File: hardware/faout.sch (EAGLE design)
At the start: 106 parts, among them IC2 MT48LC64M4A2, Q1 12MHz, Q2 ASFL, U1 LTC3419EMS, U10 REF102AU, U2 93C46B, U3 FLASH-SPI-25XXSMD1, U4 6SLX9TQG144, U5 OPA2277UA/2K5E4, U6 DAC8811DGK, U7 REF102AU, U8 OPA2277UA/2K5E4, U9 DAC8811DGK

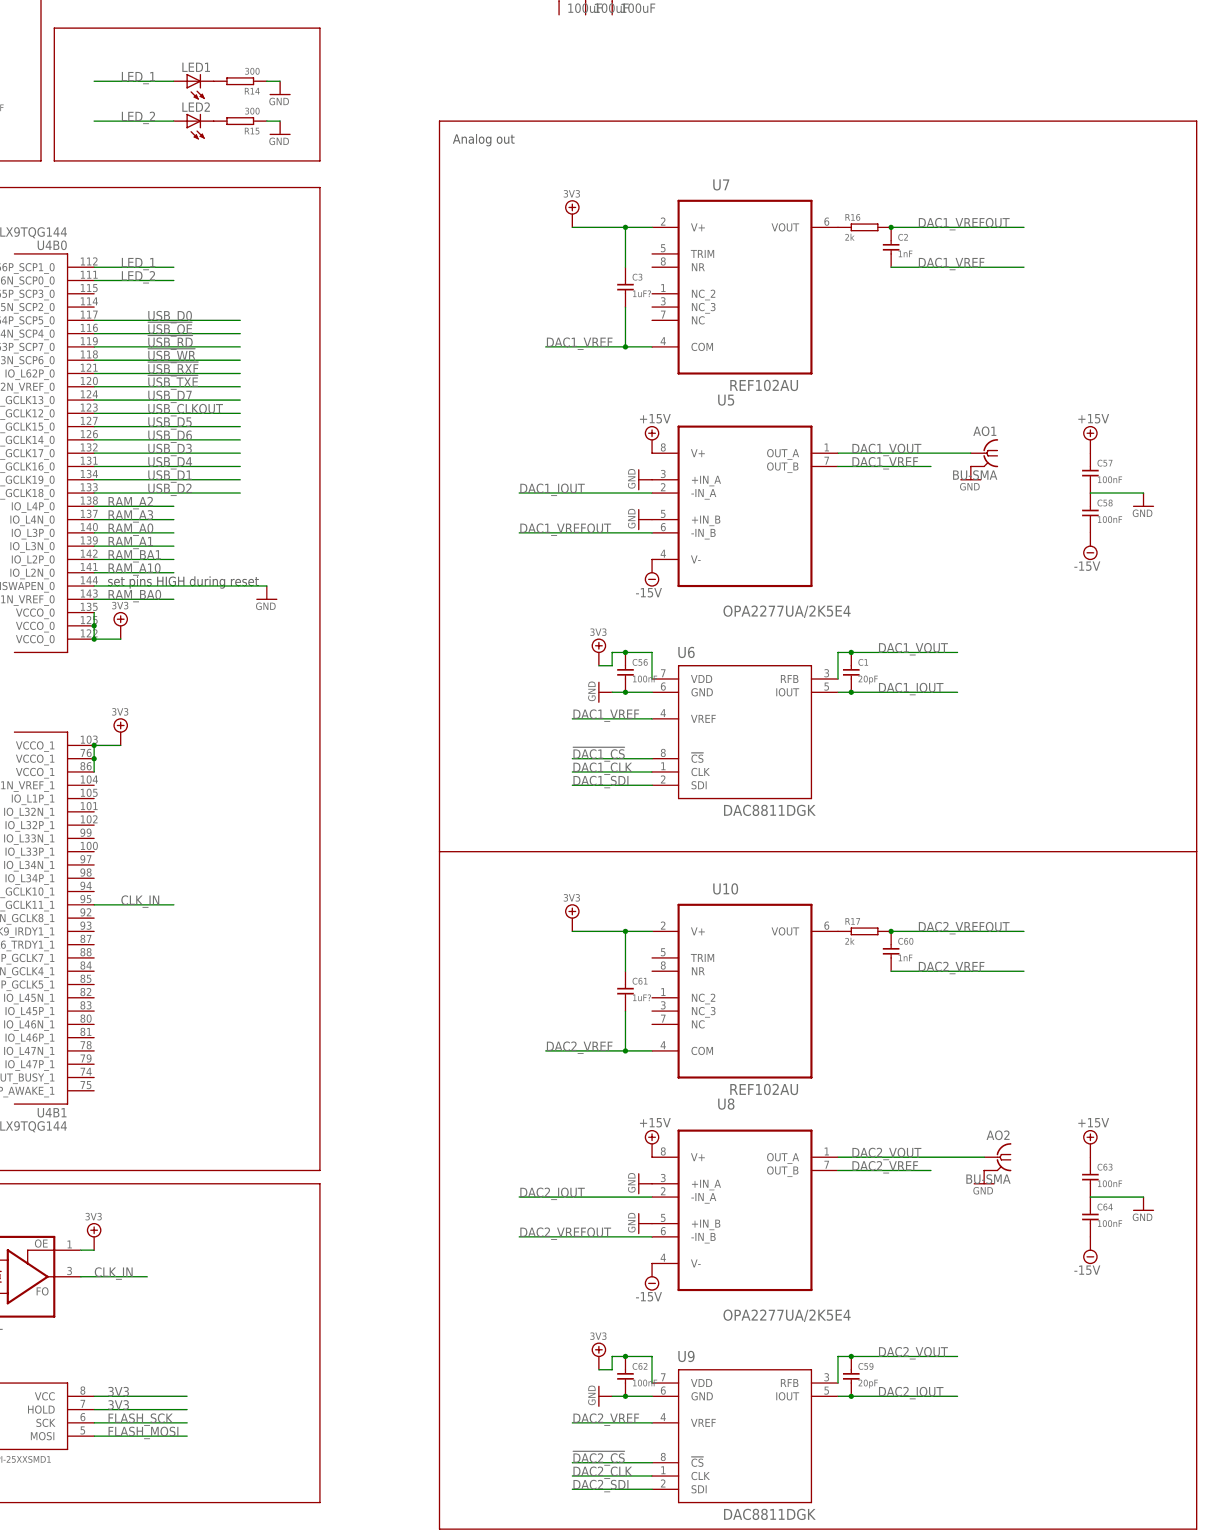
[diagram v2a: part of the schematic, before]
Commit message: Connected DACs to power and FPGA.
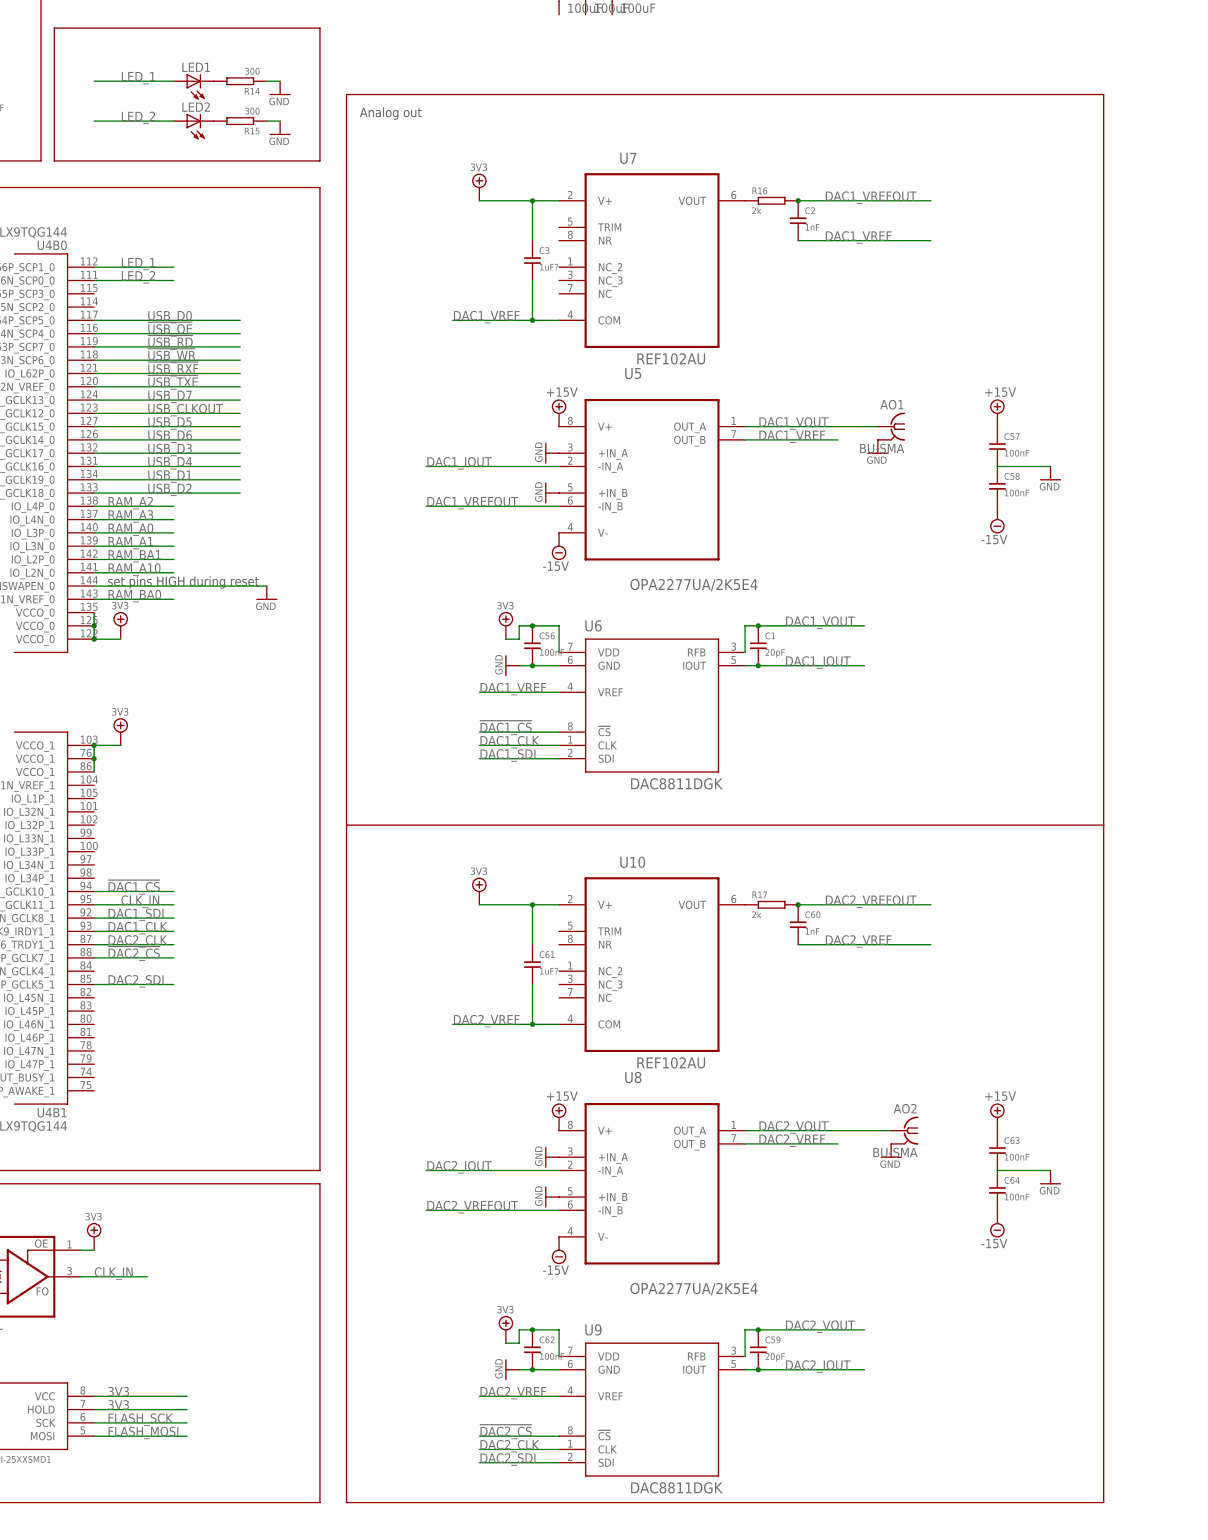
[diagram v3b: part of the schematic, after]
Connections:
- net !DAC1_CS: now also U4B1.IO_L40N_GCLK10_1
- net !DAC2_CS: now also U4B1.IO_L42P_GCLK7_1
- net DAC1_CLK: now also U4B1.IO_L41P_GCLK9_IRDY1_1
- net DAC1_SDI: now also U4B1.IO_L41N_GCLK8_1
- net DAC2_CLK: now also U4B1.IO_L42N_GCLK6_TRDY1_1
- net DAC2_SDI: now also U4B1.IO_L43P_GCLK5_1
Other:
- moved on the sheet: AO1, AO2, C1, C2, C3, C56, C57, C58, C59, C60, C61, C62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

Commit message: Add parts for ADC conversion.
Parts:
- added AI1: BU-SMA, analog_out_lib:BU-SMA
- added C65: 22uF, resistor:C-EUC1206
- added C66, C67: 100nF, faout:C_EU0603
- added U11: DAC8811DGK, faout:DAC8811DGK
- added U12: MCP1700T-2502E/TT, faout:MCP1700T-2502E/TT
- added U13: AD7980ARMZ, faout:AD7980ARMZ
- added U14: ADR435ARZ, faout:ADR435ARZ
- C1: value 20pF -> 3.3uF
- C12: value 100nF -> 10uF/10V; device faout:C_EU0603 -> faout:C_EU0805
- C17, C18: value 100nF -> 470nF
- C19, C20: value 100uF -> 4.7uF; device rcl:C-EUC1210K -> faout:C_EU0603
- C2: value 1nF -> 18pF
- C21: value 100uF -> 10nF; device rcl:C-EUC1210K -> faout:C_EU0603
- C22, C23: value 470nF -> 22uF/6V3; device faout:C_EU0603 -> faout:C_EU0805
- C24, C44: value 4.7uF -> 10nF
- C27, C33, C35, C37, C39, C45: value 4.7uF -> 470nF
- C28, C29, C31, C34, C38, C46: value 470nF -> 4.7uF
- C3: value 1uF? -> 18pF
- C4: value 3.3uF -> 4.7uF
- C5: value 18pF -> 100nF
- C50, C52: value 10nF -> 1uF?
- C51: value 10nF -> 100nF
- C53: value 10uF/10V -> 100nF; device faout:C_EU0805 -> faout:C_EU0603
- C54, C55: value 22uF/6V3 -> 1uF; device faout:C_EU0805 -> faout:C_EU0603
- C57, C58: value 100nF -> 20pF
- C59: value 20pF -> 1nF
- C6: value 18pF -> 4.7uF
- C61: value 1uF? -> 100nF
- C7, C9: value 4.7uF -> 100nF
- IC1: value (none) -> MT48LC64M4A2; device ftdichip-3:FT2232HL -> faout:MT48LC64M4A2
- IC2: value MT48LC64M4A2 -> (none); device faout:MT48LC64M4A2 -> ftdichip-3:FT2232HL
- L1, L2: value 3.3uH -> (none); device Bogdan_Commons:L_VLS3015 -> faout:R_EU0603
- L3, L4: value (none) -> 3.3uH; device faout:R_EU0603 -> Bogdan_Commons:L_VLS3015
- R1, R2, R4: value 1K5 1% -> 10k
- R10: value 12k -> 1K5 1%
- R11: value 0 -> 6K8 1%
- R12: value 0 -> 1K5 1%
- R3: value 6K8 1% -> 2.2k
- R5: value 10k -> 1k
- R6: value 10k -> 12k
- R7: value 2.2k -> 0
- R8: value 10k -> 0
- R9: value 1k -> 1K5 1%
- U1: value LTC3419EMS -> 93C46B; device Bogdan_Commons:LTC3419EMS -> Bogdan_Commons:DIGITAL-EEPROM-MICROWIRE-6P_SOT23
- U10, U7: value REF102AU -> OPA2277UA/2K5E4; device faout:REF102AU -> faout:OPA2277UA/2K5E4
- U2: value 93C46B -> LTC3419EMS; device Bogdan_Commons:DIGITAL-EEPROM-MICROWIRE-6P_SOT23 -> Bogdan_Commons:LTC3419EMS
- U5: value OPA2277UA/2K5E4 -> AD8220ARMZ; device faout:OPA2277UA/2K5E4 -> faout:AD8220ARMZ
- U6, U9: value DAC8811DGK -> REF102AU; device faout:DAC8811DGK -> faout:REF102AU
- U8: value OPA2277UA/2K5E4 -> DAC8811DGK; device faout:OPA2277UA/2K5E4 -> faout:DAC8811DGK
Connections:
- new net 2V5: C55.P$1, U12.VOUT, U13.VDD
- new net ADC1_CNV: U13.CNV
- new net ADC1_REF: C65.1, U13.REF, U14.VOUT
- new net ADC1_SCK: U13.SCK
- new net ADC1_SDI: U13.SDI
- new net ADC1_SDO: U13.SDO
- new net N$11: AI1.2, U5.-IN
- new net N$12: C54.P$1, U12.VIN
- new net N$9: AI1.1, U5.+IN
- net !DAC1_CS: now also U8.!CS; no longer U6.!CS
- net !DAC2_CS: now also U11.!CS; no longer U9.!CS
- net !RAM_CAS: now also IC1G$1.!CAS; no longer IC2G$1.!CAS
- net !RAM_RAS: now also IC1G$1.!RAS; no longer IC2G$1.!RAS
- net !RAM_WE: now also IC1G$1.!WE; no longer IC2G$1.!WE
- net !USB_OE: now also IC2.ACBUS6; no longer IC1.ACBUS6
- net !USB_RD: now also IC2.ACBUS2; no longer IC1.ACBUS2
- net !USB_RESET: now also IC2.-RESET, R5.P$1; no longer IC1.-RESET, R9.P$1
- net !USB_RXF: now also IC2.ACBUS0; no longer IC1.ACBUS0
- net !USB_TXE: now also IC2.ACBUS1; no longer IC1.ACBUS1
- net !USB_WR: now also IC2.ACBUS3; no longer IC1.ACBUS3
- net +15V: now also C56.P$1, C61.P$1, C66.P$1, U10.V+, U14.VIN, U5.+VS, U7.V+; no longer C57.P$1, U5.V+, U8.V+
- net -15V: now also C62.P$2, C67.P$2, U10.V-, U5.-VS, U7.V-; no longer C58.P$2, U5.V-, U8.V-
- net 1V2: now also C23.P$1, C26.P$1, C28.P$1, C30.P$1, C31.P$1, L4.2, R12.P$2; no longer C34.P$1, C35.P$1, C36.P$1, C37.P$1, C55.P$1, L2.2, R4.P$2
- net 1V8: now also C1.P$1, C10.P$1, C11.P$1, C9.P$1, IC2.VCORE@1, IC2.VCORE@2, IC2.VCORE@3, IC2.VREGOUT; no longer C12.P$1, C13.P$1, C14.P$1, C4.P$1, IC1.VCORE@1, IC1.VCORE@2, IC1.VCORE@3, IC1.VREGOUT
- net 3V3: now also C13.P$1, C14.P$1, C19.P$1, C20.P$1, C21.P$1, C34.P$1, C35.P$1, C36.P$1, C37.P$1, C5.P$1, C53.P$1, IC1P.VDD@1, IC1P.VDD@2, IC1P.VDD@3, IC1P.VDDQ@1, IC1P.VDDQ@2, IC1P.VDDQ@3, IC1P.VDDQ@4, IC2.ACBUS4, IC2.VCCIO@1, IC2.VCCIO@2, IC2.VCCIO@3, IC2.VCCIO@4, IC2.VREGIN, L1.P$1, L2.P$1, L3.2, R1.P$2, R11.P$2, R2.P$2, R4.P$2, U1.VCC, U11.VDD, U2.RUN2, U6.V+, U8.VDD, U9.V+; no longer C23.P$1, C26.P$1, C28.P$1, C3.P$1, C30.P$1, C31.P$1, C54.P$1, C56.P$1, C61.P$1, C62.P$1, C8.P$1, IC1.ACBUS4, IC1.VCCIO@1, IC1.VCCIO@2, IC1.VCCIO@3, IC1.VCCIO@4, IC1.VREGIN, IC2P.VDD@1, IC2P.VDD@2, IC2P.VDD@3, IC2P.VDDQ@1, IC2P.VDDQ@2, IC2P.VDDQ@3, IC2P.VDDQ@4, L1.2, L3.P$1, L4.P$1, R3.P$2, R6.P$2, R8.P$2, R9.P$2, U1.RUN2, U10.V+, U2.VCC, U6.VDD, U7.V+, U9.VDD
- net 5V0: now also C12.P$1, R7.P$1, U2.MODE, U2.RUN1, U2.VIN; no longer C53.P$1, R12.P$1, U1.MODE, U1.RUN1, U1.VIN
- net DAC1_CLK: now also U8.CLK; no longer U6.CLK
- net DAC1_IOUT: now also C57.P$2, U7.-IN_A, U8.IOUT; no longer C1.P$2, U5.-IN_A, U6.IOUT
- net DAC1_SDI: now also U8.SDI; no longer U6.SDI
- net DAC1_VOUT: now also C57.P$1, U7.OUT_A, U8.RFB; no longer C1.P$1, U5.OUT_A, U6.RFB
- net DAC1_VREF: now also C50.P$2, C59.P$2, U6.COM, U7.OUT_B, U8.VREF; no longer C2.P$2, C3.P$2, U5.OUT_B, U6.VREF, U7.COM
- net DAC1_VREFOUT: now also C59.P$1, U7.-IN_B; no longer C2.P$1, U5.-IN_B
- net DAC2_CLK: now also U11.CLK; no longer U9.CLK
- net DAC2_IOUT: now also C58.P$2, U10.-IN_A, U11.IOUT; no longer C59.P$2, U8.-IN_A, U9.IOUT
- net DAC2_SDI: now also U11.SDI; no longer U9.SDI
- net DAC2_VOUT: now also C58.P$1, U10.OUT_A, U11.RFB; no longer C59.P$1, U8.OUT_A, U9.RFB
- net DAC2_VREF: now also C52.P$2, U10.OUT_B, U11.VREF, U9.COM; no longer C61.P$2, U10.COM, U8.OUT_B, U9.VREF
- net DAC2_VREFOUT: now also U10.-IN_B; no longer U8.-IN_B
- net EECS: now also IC2.EECS, R1.P$1, U1.CS; no longer IC1.EECS, R5.P$1, U2.CS
- net EEDATA: now also IC2.EEDATA, R3.P$1, R4.P$1, U1.DI; no longer IC1.EEDATA, R7.P$1, R8.P$1, U2.DI
- net EESK: now also IC2.EESK, R2.P$1, U1.CLK; no longer IC1.EESK, R6.P$1, U2.CLK
- net FB_1V2: now also R10.P$2, R12.P$1, U2.VFB2; no longer R2.P$2, R4.P$1, U1.VFB2
- net FB_3V3: now also R11.P$1, R9.P$2, U2.VFB1; no longer R1.P$2, R3.P$1, U1.VFB1
- net GND: now also C1.P$2, C19.P$2, C2.P$2, C20.P$2, C21.P$2, C3.P$2, C61.P$2, C62.P$1, C65.2, C66.P$2, C67.P$1, IC1P.VSS@1, IC1P.VSS@2, IC1P.VSS@3, IC1P.VSSQ@1, IC1P.VSSQ@2, IC1P.VSSQ@3, IC1P.VSSQ@4, IC2.AGND, IC2.GND@1, IC2.GND@2, IC2.GND@3, IC2.GND@4, IC2.GND@5, IC2.GND@6, IC2.GND@7, IC2.GND@8, IC2.TEST, R10.P$1, R6.P$2, R8.P$1, R9.P$1, U1.GND, U10.+IN_A, U10.+IN_B, U11.GND, U12.GND, U13.GND, U13.IN-, U14.GND, U2.GND@5, U2.GND@6, U5.REF, U7.+IN_A, U7.+IN_B, U8.GND; no longer C50.P$2, C52.P$2, C57.P$2, C58.P$1, C62.P$2, IC1.AGND, IC1.GND@1, IC1.GND@2, IC1.GND@3, IC1.GND@4, IC1.GND@5, IC1.GND@6, IC1.GND@7, IC1.GND@8, IC1.TEST, IC2P.VSS@1, IC2P.VSS@2, IC2P.VSS@3, IC2P.VSSQ@1, IC2P.VSSQ@2, IC2P.VSSQ@3, IC2P.VSSQ@4, R1.P$1, R10.P$2, R11.P$1, R2.P$1, U1.GND@5, U1.GND@6, U2.GND, U5.+IN_A, U5.+IN_B, U6.GND, U8.+IN_A, U8.+IN_B, U9.GND
- net N$1: now also C2.P$1, IC2.XTIN; no longer C5.P$1, IC1.XTIN
- net N$10: now also U6.VOUT; no longer U7.VOUT
- net N$2: now also C3.P$1, IC2.XTOUT; no longer C6.P$1, IC1.XTOUT
- net N$5: now also C4.P$1, IC2.VPHY, L2.P$2; no longer C10.P$1, IC1.VPHY, L4.P$2
- net N$6: now also R3.P$2, U1.DO; no longer R7.P$2, U2.DO
- net N$7: now also C6.P$1, C8.P$1, IC2.VPLL, L1.P$2; no longer C11.P$1, C9.P$1, IC1.VPLL, L3.P$2
- net N$8: now also U9.VOUT; no longer U10.VOUT
- net RAM_A0: now also IC1G$1.A0; no longer IC2G$1.A0
- net RAM_A1: now also IC1G$1.A1; no longer IC2G$1.A1
- net RAM_A10: now also IC1G$1.A10; no longer IC2G$1.A10
- net RAM_A11: now also IC1G$1.A11; no longer IC2G$1.A11
- net RAM_A12: now also IC1G$1.A12; no longer IC2G$1.A12
- net RAM_A2: now also IC1G$1.A2; no longer IC2G$1.A2
- net RAM_A3: now also IC1G$1.A3; no longer IC2G$1.A3
- net RAM_A4: now also IC1G$1.A4; no longer IC2G$1.A4
- net RAM_A5: now also IC1G$1.A5; no longer IC2G$1.A5
- net RAM_A6: now also IC1G$1.A6; no longer IC2G$1.A6
- net RAM_A7: now also IC1G$1.A7; no longer IC2G$1.A7
- net RAM_A8: now also IC1G$1.A8; no longer IC2G$1.A8
- net RAM_A9: now also IC1G$1.A9; no longer IC2G$1.A9
- net RAM_BA0: now also IC1G$1.BA0; no longer IC2G$1.BA0
- net RAM_BA1: now also IC1G$1.BA1; no longer IC2G$1.BA1
- net RAM_CKE: now also IC1G$1.CKE; no longer IC2G$1.CKE
- net RAM_CLK: now also IC1G$1.CLK; no longer IC2G$1.CLK
- net RAM_CS: now also IC1G$1.\CS; no longer IC2G$1.\CS
- net RAM_DQ0: now also IC1G$1.DQ0; no longer IC2G$1.DQ0
- net RAM_DQ1: now also IC1G$1.DQ1; no longer IC2G$1.DQ1
- net RAM_DQ10: now also IC1G$1.DQ10; no longer IC2G$1.DQ10
- net RAM_DQ11: now also IC1G$1.DQ11; no longer IC2G$1.DQ11
- net RAM_DQ12: now also IC1G$1.DQ12; no longer IC2G$1.DQ12
- net RAM_DQ13: now also IC1G$1.DQ13; no longer IC2G$1.DQ13
- net RAM_DQ14: now also IC1G$1.DQ14; no longer IC2G$1.DQ14
- net RAM_DQ15: now also IC1G$1.DQ15; no longer IC2G$1.DQ15
- net RAM_DQ2: now also IC1G$1.DQ2; no longer IC2G$1.DQ2
- net RAM_DQ3: now also IC1G$1.DQ3; no longer IC2G$1.DQ3
- net RAM_DQ4: now also IC1G$1.DQ4; no longer IC2G$1.DQ4
- net RAM_DQ5: now also IC1G$1.DQ5; no longer IC2G$1.DQ5
- net RAM_DQ6: now also IC1G$1.DQ6; no longer IC2G$1.DQ6
- net RAM_DQ7: now also IC1G$1.DQ7; no longer IC2G$1.DQ7
- net RAM_DQ8: now also IC1G$1.DQ8; no longer IC2G$1.DQ8
- net RAM_DQ9: now also IC1G$1.DQ9; no longer IC2G$1.DQ9
- net RAM_DQMH: now also IC1G$1.DQMH; no longer IC2G$1.DQMH
- net RAM_DQML: now also IC1G$1.DQML; no longer IC2G$1.DQML
- net SW_1V2: now also L4.1, U2.SW2; no longer L2.1, U1.SW2
- net SW_3V3: now also L3.1, U2.SW1; no longer L1.1, U1.SW1
- net TCK: now also IC2.BDBUS0; no longer IC1.BDBUS0
- net TDI: now also IC2.BDBUS1; no longer IC1.BDBUS1
- net TDO: now also IC2.BDBUS2; no longer IC1.BDBUS2
- net TMS: now also IC2.BDBUS3; no longer IC1.BDBUS3
- net USB_CLKOUT: now also IC2.ACBUS5; no longer IC1.ACBUS5
- net USB_D0: now also IC2.ADBUS0; no longer IC1.ADBUS0
- net USB_D1: now also IC2.ADBUS1; no longer IC1.ADBUS1
- net USB_D2: now also IC2.ADBUS2; no longer IC1.ADBUS2
- net USB_D3: now also IC2.ADBUS3; no longer IC1.ADBUS3
- net USB_D4: now also IC2.ADBUS4; no longer IC1.ADBUS4
- net USB_D5: now also IC2.ADBUS5; no longer IC1.ADBUS5
- net USB_D6: now also IC2.ADBUS6; no longer IC1.ADBUS6
- net USB_D7: now also IC2.ADBUS7; no longer IC1.ADBUS7
- net USB_DM: now also IC2.D-; no longer IC1.D-
- net USB_DP: now also IC2.D+; no longer IC1.D+
- net USB_GND: now also R8.P$2; no longer R11.P$2
- net USB_REF: now also IC2.REF, R6.P$1; no longer IC1.REF, R10.P$1
- net USB_V: now also R7.P$2; no longer R12.P$2
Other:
- moved on the sheet: C1, C10, C11, C12, C13, C14, C15, C16, C17, C18, C19, C2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

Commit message: Finalize USB and ADC layout.
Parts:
- added C68, C69: 100nF, faout:C_EU0603
- added C70: 114pF, faout:C_EU0603
- added C71: 11.4pF, faout:C_EU0603
- added JP3: (no value), pinhead:PINHD-1X2
- added L5: (no value), faout:R_EU0603
- added R18, R19: 7.47k, faout:R_EU0603
- added R20: 134k, faout:R_EU0603
- added U15: AD8627AKSZ-R2, faout:AD8627AKSZ-R2
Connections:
- removed net +15V: C56.P$1, C61.P$1, C63.P$1, C66.P$1, U10.V+, U14.VIN, U5.+VS, U7.V+
- removed net -15V: C62.P$2, C64.P$2, C67.P$2, U10.V-, U5.-VS, U7.V-
- new net A+12V: C56.P$1, C61.P$1, C63.P$1, C66.P$1, C68.P$1, U10.V+, U14.VIN, U15.V+, U5.+VS, U7.V+
- new net A+3V3: C50.P$1, C51.P$1, C52.P$1, C53.P$1, C54.P$1, U11.VDD, U12.VIN, U13.VIO, U6.V+, U8.VDD, U9.V+
- new net A-12V: C62.P$2, C64.P$2, C67.P$2, C69.P$2, U10.V-, U15.V-, U5.-VS, U7.V-
- new net N$13: R18.P$2, U5.VOUT
- new net N$14: C70.P$2, R18.P$1, R19.P$2, R20.P$1
- new net N$15: C71.P$1, R20.P$2, U15.+IN
- new net N$16: L5.P$1, USB1.SHD@4
- net !USB_RESET: now also JP3.1
- net 3V3: no longer C50.P$1, C51.P$1, C52.P$1, C53.P$1, U11.VDD, U6.V+, U8.VDD, U9.V+
- net ADC1_CNV: now also U4B1.IO_L33P_1
- net ADC1_SCK: now also U4B1.IO_L34P_1
- net ADC1_SDI: now also U4B1.IO_L34N_1
- net ADC1_SDO: now also U4B1.IO_L33N_1
- net GND: now also C68.P$2, C69.P$1, C71.P$2, JP3.2, L5.P$2, R19.P$1
- net N$12: now also C70.P$1, U13.IN+, U15.-IN, U15.OUT_A; no longer C54.P$1, U12.VIN
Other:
- note added: "1MHz Filter"
- note added: "Analog in"
- moved on the sheet: AI1, AO1, AO2, C50, C51, C52, C54, C55, C56, C57, C59, C60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
